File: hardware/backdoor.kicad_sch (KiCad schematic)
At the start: 30 parts, among them J1 E1, Q1 J201, U1 OP07

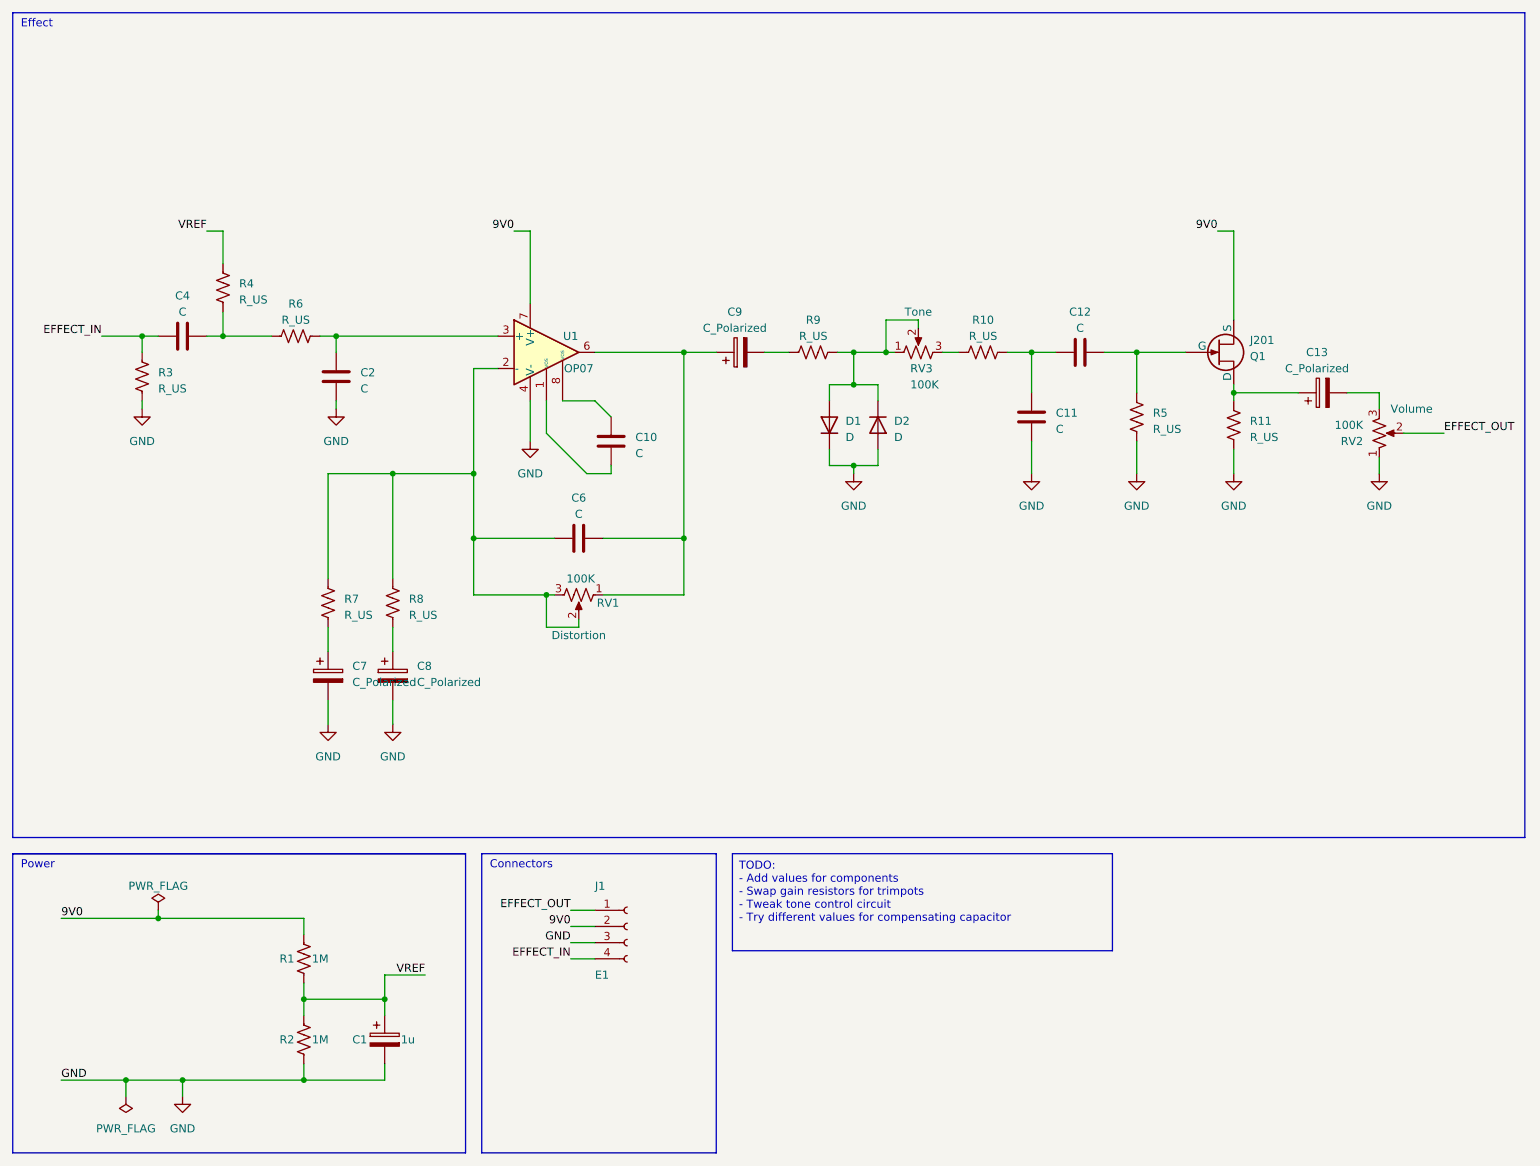
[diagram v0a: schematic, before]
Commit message: Add values after experimenting on the breadboard
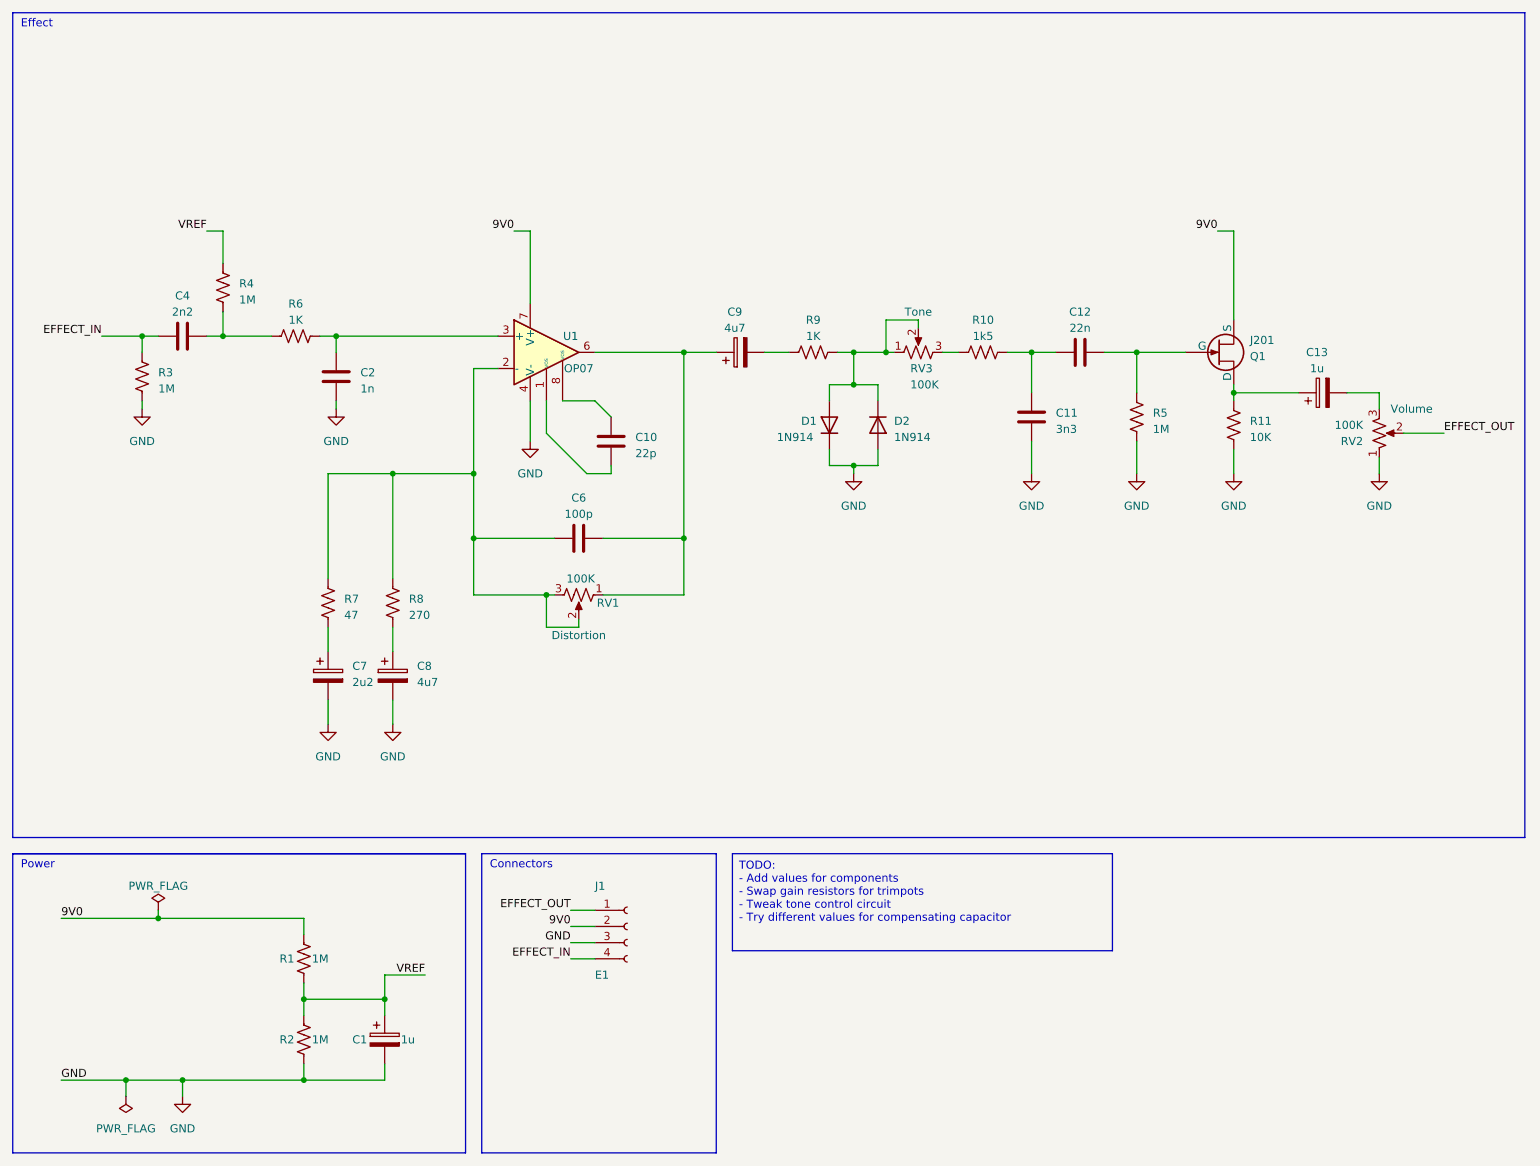
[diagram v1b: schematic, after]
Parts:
- C10: value C -> 22p
- C11: value C -> 3n3
- C12: value C -> 22n
- C13: value C_Polarized -> 1u
- C2: value C -> 1n
- C4: value C -> 2n2
- C6: value C -> 100p
- C7: value C_Polarized -> 2u2
- C8, C9: value C_Polarized -> 4u7
- D1, D2: value D -> 1N914
- R10: value R_US -> 1k5
- R11: value R_US -> 10K
- R3, R4, R5: value R_US -> 1M
- R6, R9: value R_US -> 1K
- R7: value R_US -> 47
- R8: value R_US -> 270
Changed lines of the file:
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@@
       (effects (font (size 1.27 1.27)) (justify left))
     )
-    (property "Value" "C_Polarized" (at 76.2 117.856 0)
+    (property "Value" "4u7" (at 76.2 117.856 0)
       (effects (font (size 1.27 1.27)) (justify left))
     )
@@
       (effects (font (size 1.27 1.27)))
     )
-    (property "Value" "C" (at 101.6 91.44 90)
+    (property "Value" "100p" (at 101.6 91.44 90)
       (effects (font (size 1.27 1.27)))
     )
@@
       (effects (font (size 1.27 1.27)))
     )
-    (property "Value" "C_Polarized" (at 217.551 68.58 90)
+    (property "Value" "1u" (at 217.551 68.58 90)
       (effects (font (size 1.27 1.27)))
     )
@@
       (effects (font (size 1.27 1.27)) (justify left))
     )
-    (property "Value" "R_US" (at 207.01 79.375 0)
+    (property "Value" "10K" (at 207.01 79.375 0)
       (effects (font (size 1.27 1.27)) (justify left))
     )
@@
       (effects (font (size 1.27 1.27)))
     )
-    (property "Value" "R_US" (at 165.1 63.5 90)
+    (property "Value" "1k5" (at 165.1 63.5 90)
       (effects (font (size 1.27 1.27)))
     )
@@
       (effects (font (size 1.27 1.27)))
     )
-    (property "Value" "C_Polarized" (at 126.111 62.23 90)
+    (property "Value" "4u7" (at 126.111 62.23 90)
       (effects (font (size 1.27 1.27)))
     )
@@
       (effects (font (size 1.27 1.27)))
     )
-    (property "Value" "R_US" (at 57.15 60.96 90)
+    (property "Value" "1K" (at 57.15 60.96 90)
       (effects (font (size 1.27 1.27)))
     )
@@
       (effects (font (size 1.27 1.27)) (justify left))
     )
-    (property "Value" "D" (at 151.13 79.375 90)
+    (property "Value" "1N914" (at 151.13 79.375 90)
       (effects (font (size 1.27 1.27)) (justify left))
     )
@@
       (effects (font (size 1.27 1.27)) (justify left))
     )
-    (property "Value" "C" (at 67.31 71.755 0)
+    (property "Value" "1n" (at 67.31 71.755 0)
       (effects (font (size 1.27 1.27)) (justify left))
     )
@@
       (effects (font (size 1.27 1.27)) (justify left))
     )
-    (property "Value" "C_Polarized" (at 66.04 117.856 0)
+    (property "Value" "2u2" (at 66.04 117.856 0)
       (effects (font (size 1.27 1.27)) (justify left))
     )
@@
       (effects (font (size 1.27 1.27)) (justify left))
     )
-    (property "Value" "C" (at 176.53 78.105 0)
+    (property "Value" "3n3" (at 176.53 78.105 0)
       (effects (font (size 1.27 1.27)) (justify left))
     )
@@
       (effects (font (size 1.27 1.27)) (justify left))
     )
-    (property "Value" "R_US" (at 48.26 57.785 0)
+    (property "Value" "1M" (at 48.26 57.785 0)
       (effects (font (size 1.27 1.27)) (justify left))
     )
@@
       (effects (font (size 1.27 1.27)))
     )
-    (property "Value" "C" (at 39.37 59.69 90)
+    (property "Value" "2n2" (at 39.37 59.69 90)
       (effects (font (size 1.27 1.27)))
     )
@@
       (effects (font (size 1.27 1.27)) (justify left))
     )
-    (property "Value" "R_US" (at 191.77 78.105 0)
+    (property "Value" "1M" (at 191.77 78.105 0)
       (effects (font (size 1.27 1.27)) (justify left))
     )
@@
       (effects (font (size 1.27 1.27)))
     )
-    (property "Value" "R_US" (at 138.43 63.5 90)
+    (property "Value" "1K" (at 138.43 63.5 90)
       (effects (font (size 1.27 1.27)))
     )
@@
       (effects (font (size 1.27 1.27)) (justify left))
     )
-    (property "Value" "R_US" (at 74.93 107.315 0)
+    (property "Value" "270" (at 74.93 107.315 0)
       (effects (font (size 1.27 1.27)) (justify left))
     )
@@
       (effects (font (size 1.27 1.27)) (justify right))
     )
-    (property "Value" "C" (at 110.49 81.915 0)
+    (property "Value" "22p" (at 110.49 81.915 0)
       (effects (font (size 1.27 1.27)) (justify right))
     )
@@
   (symbol (lib_id "Device:D") (at 140.97 77.47 90) (unit 1)
     (in_bom yes) (on_board yes) (dnp no)
-    (property "Reference" "D1" (at 143.51 76.835 90)
+    (property "Reference" "D1" (at 136.525 76.835 90)
       (effects (font (size 1.27 1.27)) (justify right))
     )
-    (property "Value" "D" (at 143.51 79.375 90)
+    (property "Value" "1N914" (at 132.715 79.375 90)
       (effects (font (size 1.27 1.27)) (justify right))
     )
@@
       (effects (font (size 1.27 1.27)))
     )
-    (property "Value" "C" (at 180.34 62.23 90)
+    (property "Value" "22n" (at 180.34 62.23 90)
       (effects (font (size 1.27 1.27)))
     )
@@
       (effects (font (size 1.27 1.27)) (justify left))
     )
-    (property "Value" "R_US" (at 35.56 71.755 0)
+    (property "Value" "1M" (at 35.56 71.755 0)
       (effects (font (size 1.27 1.27)) (justify left))
     )
@@
       (effects (font (size 1.27 1.27)) (justify left))
     )
-    (property "Value" "R_US" (at 64.77 107.315 0)
-      (effects (font (size 1.27 1.27)) (justify left))
-    )
+    (property "Value" "47" (at 64.77 107.315 0)
+      (effects (font (size 1.27 1.27)) (justify left))
+    )

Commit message: initial layout and renders, bump rev to v0.02
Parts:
- RV1, RV2, RV3: value 100K -> A100K
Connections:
- net Clip: now reaches D1.2 (A), D2.1 (K), R9.2, RV3.1, RV3.2
- net OA_Inv: now reaches C6.1, R7.1, R8.1, RV1.2, RV1.3, U1.2 (-)
- net OA_Out: now reaches C6.2, C9.1, RV1.1, U1.6
- net Buffer_Out: now reaches C13.1, Q1.1 (D), R11.1
- net Pre-Volume: now reaches C13.2, RV2.3
- net OA_Comp2: now reaches C10.1, U1.1 (VOS)
- net OA_NonInv: now reaches C2.1, R6.2, U1.3 (+)
- net OA_Comp1: now reaches C10.2, U1.8 (VOS)
- net Pre-Buffer: now reaches C12.2, Q1.2 (G), R5.1
- net DC_Biased: now reaches C4.2, R4.2, R6.1

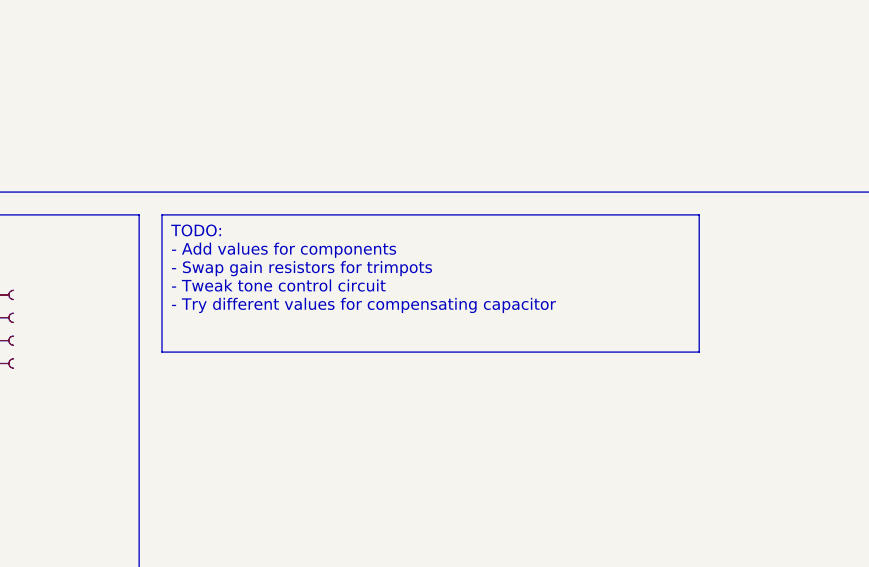
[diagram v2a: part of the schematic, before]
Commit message: Fix issue identified in v0.02 hardware
 - update schematic to use correct pin for jfet output buffer
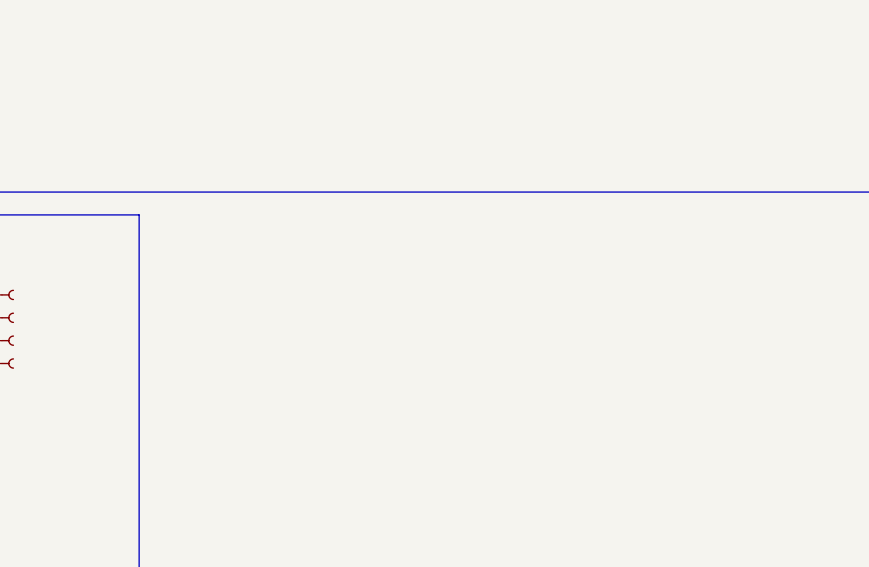
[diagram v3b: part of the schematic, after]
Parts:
- removed Q1: J201, Package_TO_SOT_THT:TO-92_Inline, symbol Simulation_SPICE:NJFET
- added Q1: J201, Package_TO_SOT_THT:TO-92_Inline, symbol Device:Q_NJFET_SDG
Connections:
- net 9V0: now also Q1.1 (S)
- net Buffer_Out: now also Q1.2 (D)
- net Pre-Buffer: now also Q1.3 (G)
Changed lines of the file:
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@@
   (title_block
     (title "\"Backdoor\" distortion effect")
-    (date "2023-03-26")
-    (rev "v0.02")
+    (date "2023-04-16")
+    (rev "v0.1")
     (comment 1 "https://github.com/whbeers/backdoor")
   )
+  (junction (at 63.5 63.5) (diameter 0) (color 0 0 0 0)
+  )
+  (junction (at 30.48 180.34) (diameter 0) (color 0 0 0 0)
+  )
+  (junction (at 58.42 167.64) (diameter 0) (color 0 0 0 0)
+  )
+  (junction (at 45.72 63.5) (diameter 0) (color 0 0 0 0)
+  )
+  (junction (at 172.72 66.04) (diameter 0) (color 0 0 0 0)
+  )
+  (junction (at 85.09 95.25) (diameter 0) (color 0 0 0 0)
+  )
+  (junction (at 58.42 180.34) (diameter 0) (color 0 0 0 0)
+  )
+  (junction (at 71.12 167.64) (diameter 0) (color 0 0 0 0)
+  )
+  (junction (at 85.09 85.09) (diameter 0) (color 0 0 0 0)
+  )
+  (junction (at 96.52 104.14) (diameter 0) (color 0 0 0 0)
+  )
+  (junction (at 118.11 95.25) (diameter 0) (color 0 0 0 0)
+  )
+  (junction (at 149.86 66.04) (diameter 0) (color 0 0 0 0)
+  )
   (junction (at 204.47 72.39) (diameter 0) (color 0 0 0 0)
   )
-  (junction (at 63.5 63.5) (diameter 0) (color 0 0 0 0)
-  )
-  (junction (at 30.48 180.34) (diameter 0) (color 0 0 0 0)
-  )
-  (junction (at 58.42 167.64) (diameter 0) (color 0 0 0 0)
-  )
-  (junction (at 45.72 63.5) (diameter 0) (color 0 0 0 0)
-  )
-  (junction (at 172.72 66.04) (diameter 0) (color 0 0 0 0)
+  (junction (at 39.37 180.34) (diameter 0) (color 0 0 0 0)
+  )
+  (junction (at 33.02 63.5) (diameter 0) (color 0 0 0 0)
+  )
+  (junction (at 35.56 154.94) (diameter 0) (color 0 0 0 0)
   )
   (junction (at 189.23 66.04) (diameter 0) (color 0 0 0 0)
   )
-  (junction (at 85.09 95.25) (diameter 0) (color 0 0 0 0)
-  )
-  (junction (at 58.42 180.34) (diameter 0) (color 0 0 0 0)
-  )
-  (junction (at 71.12 167.64) (diameter 0) (color 0 0 0 0)
-  )
-  (junction (at 85.09 85.09) (diameter 0) (color 0 0 0 0)
-  )
-  (junction (at 96.52 104.14) (diameter 0) (color 0 0 0 0)
-  )
-  (junction (at 118.11 95.25) (diameter 0) (color 0 0 0 0)
-  )
-  (junction (at 149.86 66.04) (diameter 0) (color 0 0 0 0)
-  )
-  (junction (at 39.37 180.34) (diameter 0) (color 0 0 0 0)
-  )
-  (junction (at 33.02 63.5) (diameter 0) (color 0 0 0 0)
-  )
-  (junction (at 35.56 154.94) (diameter 0) (color 0 0 0 0)
-  )
   (junction (at 144.78 83.82) (diameter 0) (color 0 0 0 0)
   )
@@
     (stroke (width 0) (type default))
   )
+  (wire (pts (xy 204.47 46.99) (xy 204.47 60.96))
+    (stroke (width 0) (type default))
+  )
   (wire (pts (xy 35.56 153.67) (xy 35.56 154.94))
     (stroke (width 0) (type default))
@@
     (stroke (width 0) (type default))
   )
+  (wire (pts (xy 71.12 167.64) (xy 58.42 167.64))
+    (stroke (width 0) (type default))
+  )
+  (wire (pts (xy 72.39 120.65) (xy 72.39 124.46))
+    (stroke (width 0) (type default))
+  )
+  (wire (pts (xy 172.72 66.04) (xy 172.72 72.39))
+    (stroke (width 0) (type default))
+  )
+  (wire (pts (xy 62.23 120.65) (xy 62.23 124.46))
+    (stroke (width 0) (type default))
+  )
   (wire (pts (xy 204.47 71.12) (xy 204.47 72.39))
     (stroke (width 0) (type default))
   )
-  (wire (pts (xy 71.12 167.64) (xy 58.42 167.64))
-    (stroke (width 0) (type default))
-  )
-  (wire (pts (xy 72.39 120.65) (xy 72.39 124.46))
-    (stroke (width 0) (type default))
-  )
-  (wire (pts (xy 172.72 66.04) (xy 172.72 72.39))
-    (stroke (width 0) (type default))
-  )
-  (wire (pts (xy 62.23 120.65) (xy 62.23 124.46))
-    (stroke (width 0) (type default))
-  )
   (wire (pts (xy 189.23 66.04) (xy 189.23 72.39))
     (stroke (width 0) (type default))
@@
     (stroke (width 0) (type default))
   )
-  (wire (pts (xy 204.47 46.99) (xy 204.47 60.96))
-    (stroke (width 0) (type default))
-  )
   (wire (pts (xy 148.59 71.12) (xy 148.59 73.66))
     (stroke (width 0) (type default))
@@
     (stroke (width 0) (type default))
     (fill (type none))
-  )
-  (text_box "TODO:\n - Add values for components\n - Swap gain resistors for trimpots\n - Tweak tone control circuit\n - Try different values for compensating capacitor"
-    (at 125.73 144.78 0) (size 59.69 15.24)
-    (stroke (width 0) (type default))
-    (fill (type none))
-    (effects (font (size 1.27 1.27)) (justify left top))
   )
   (text "Connectors" (at 87.63 147.32 0)
@@
     )
   )
-  (symbol (lib_id "Simulation_SPICE:NJFET") (at 201.93 66.04 0) (mirror x) (unit 1)
-    (in_bom yes) (on_board yes) (dnp no)
-    (property "Reference" "Q1" (at 207.01 66.675 0)
-      (effects (font (size 1.27 1.27)) (justify left))
-    )
-    (property "Value" "J201" (at 207.01 64.135 0)
-      (effects (font (size 1.27 1.27)) (justify left))
-    )
-    (property "Footprint" "Package_TO_SOT_THT:TO-92_Inline" (at 207.01 68.58 0)
-      (effects (font (size 1.27 1.27)) hide)
-    )
-    (property "Datasheet" "~" (at 201.93 66.04 0)
-      (effects (font (size 1.27 1.27)) hide)
-    )
-    (property "Sim.Device" "NJFET" (at 201.93 66.04 0)
-      (effects (font (size 1.27 1.27)) hide)
-    )
-    (property "Sim.Type" "SHICHMANHODGES" (at 201.93 66.04 0)
-      (effects (font (size 1.27 1.27)) hide)
-    )
-    (property "Sim.Pins" "1=D 2=G 3=S" (at 201.93 66.04 0)
-      (effects (font (size 1.27 1.27)) hide)
-    )
-    (pin "1")
-    (pin "2")
-    (pin "3")
-    (instances
-      (project "backdoor"
-        (path "/06c31094-e1d9-4937-9b94-9c0ddf493ee1"
-          (reference "Q1") (unit 1)
-        )
-      )
-    )
-  )
   (symbol (lib_id "power:GND") (at 62.23 124.46 0) (unit 1)
     (in_bom yes) (on_board yes) (dnp no) (fields_autoplaced)
@@
         )
       )
+    )
+  )
+  (symbol (lib_id "Device:Q_NJFET_SDG") (at 201.93 66.04 0) (mirror x) (unit 1)
+    (in_bom yes) (on_board yes) (dnp no)
+    (property "Reference" "Q1" (at 207.01 66.675 0)
+      (effects (font (size 1.27 1.27)) (justify left))
+    )
+    (property "Value" "J201" (at 207.01 64.135 0)
+      (effects (font (size 1.27 1.27)) (justify left))
+    )
+    (property "Footprint" "Package_TO_SOT_THT:TO-92_Inline" (at 207.01 68.58 0)
+      (effects (font (size 1.27 1.27)) hide)
+    )
+    (property "Datasheet" "~" (at 201.93 66.04 0)
+      (effects (font (size 1.27 1.27)) hide)
+    )
+    (pin "1")
+    (pin "2")
+    (pin "3")
+    (instances
+      (project "backdoor"
+        (path "/06c31094-e1d9-4937-9b94-9c0ddf493ee1"
+          (reference "Q1") (unit 1)
+        )
+      )
